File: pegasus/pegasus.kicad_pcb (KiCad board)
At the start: 2 copper layers, 1 part

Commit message: updated cache and added backup files
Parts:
- removed MPL3115A2: Altimeter, Adafruit_MPL3115A2:1x07
- added IC1: Adafruit_MPL3115A2, Adafruit_MPL3115A2:1x07, F.Cu at (139.7, 119.4)
- added IC2: Adafruit-BNO055-PCB, Adafruit_BNO055:adafruit_, F.Cu at (71.1, 85.2)
- added IC3: L70B-M39, Quectel_L70B-M39:1x18, F.Cu at (165.1, 111.8)
- added IC4: RFD900, RFD900:1x28, F.Cu at (161.8, 67.6)
- added J1: Conn_01x02_Female, Connector_PinHeader_2.00mm:PinHeader_1x02_P2.00mm_Horizontal, F.Cu at (88.9, 127.0)
- added J2: Conn_01x02_Female, Connector_PinHeader_2.00mm:PinHeader_1x02_P2.00mm_Horizontal, F.Cu at (78.7, 106.7)
- added J3: Conn_01x02_Female, Connector_PinHeader_2.00mm:PinHeader_1x02_P2.00mm_Horizontal, F.Cu at (94.0, 109.2)
- added U1: Teensy4.1, Teensy_4.1:Teensy_4.1, F.Cu at (114.3, 48.3)

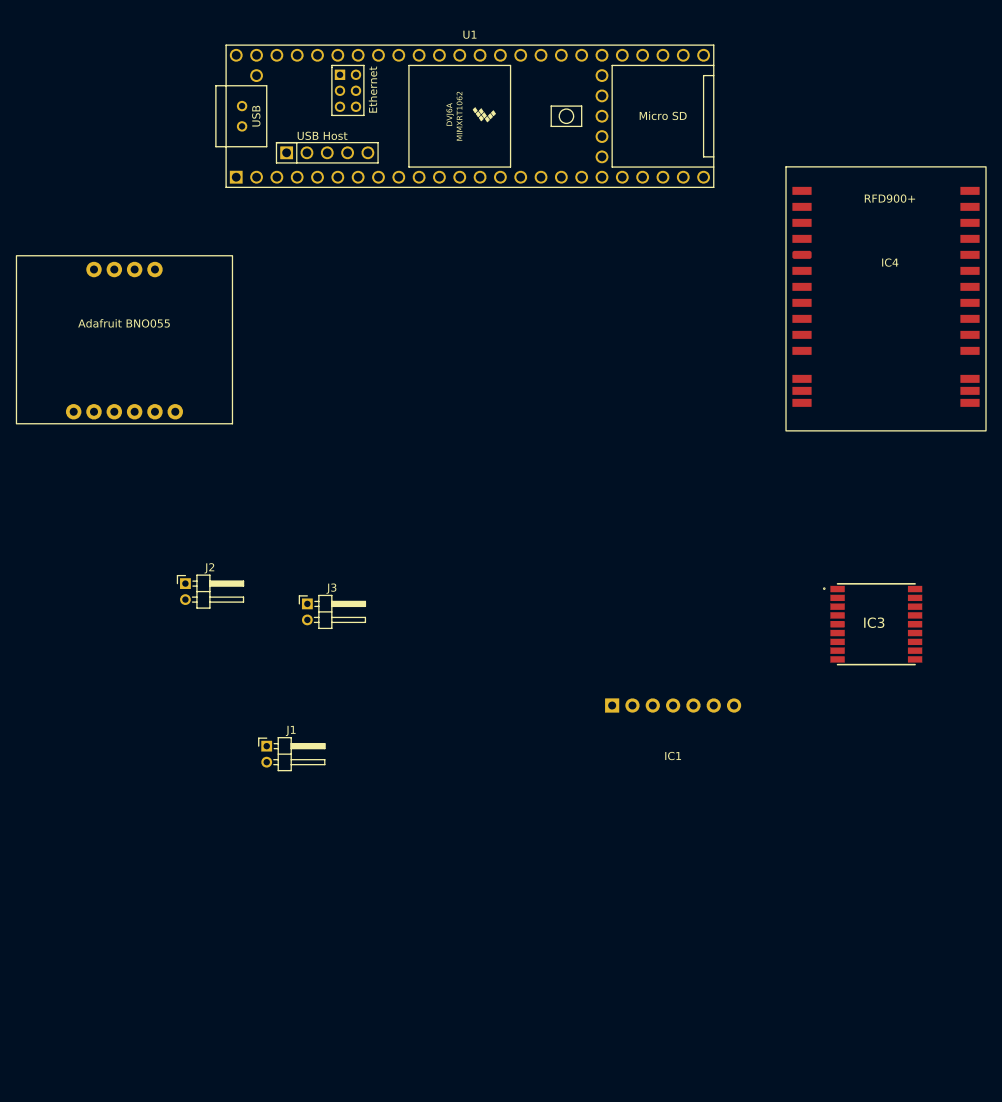
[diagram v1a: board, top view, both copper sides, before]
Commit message: outlined approximate geometry of pcb and made some connections
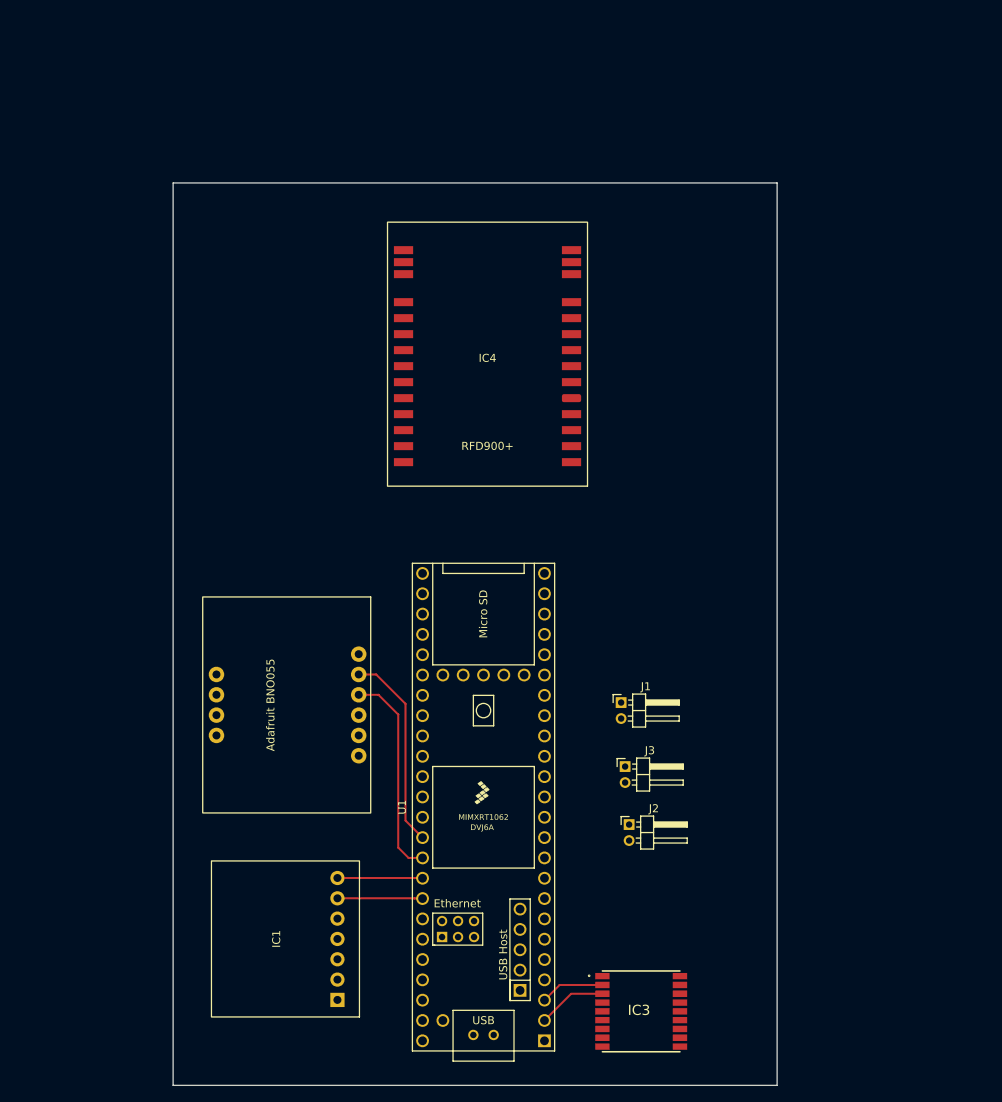
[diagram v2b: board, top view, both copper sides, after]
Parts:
- moved U1 86.4 mm to (116.0, 134.6), turned to 90 degrees
- moved J2 63.1 mm to (134.2, 136.8)
- moved IC3 56.6 mm to (135.7, 160.2)
- moved IC1 54.6 mm to (95.2, 151.1), turned to 90 degrees
- moved IC2 46.9 mm to (100.4, 121.8), turned to 90 degrees
- moved J1 44.6 mm to (133.2, 121.5)
- moved J3 44.6 mm to (133.7, 129.6)
- moved IC4 43.1 mm to (121.0, 81.5), turned to 180 degrees
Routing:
- net Net-(IC2-Pad4)_1: track 0.00 -> 26.2 mm
- net Net-(IC2-Pad5)_1: track 0.00 -> 25.0 mm
- net Net-(IC1-Pad7): track 0.00 -> 10.7 mm
- net Net-(IC1-Pad6): track 0.00 -> 10.7 mm
- net Net-(IC3-Pad3): track 0.00 -> 8.62 mm
- net Net-(IC3-Pad2): track 0.00 -> 8.02 mm
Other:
- board outline added: 75.5 x 112.8 mm

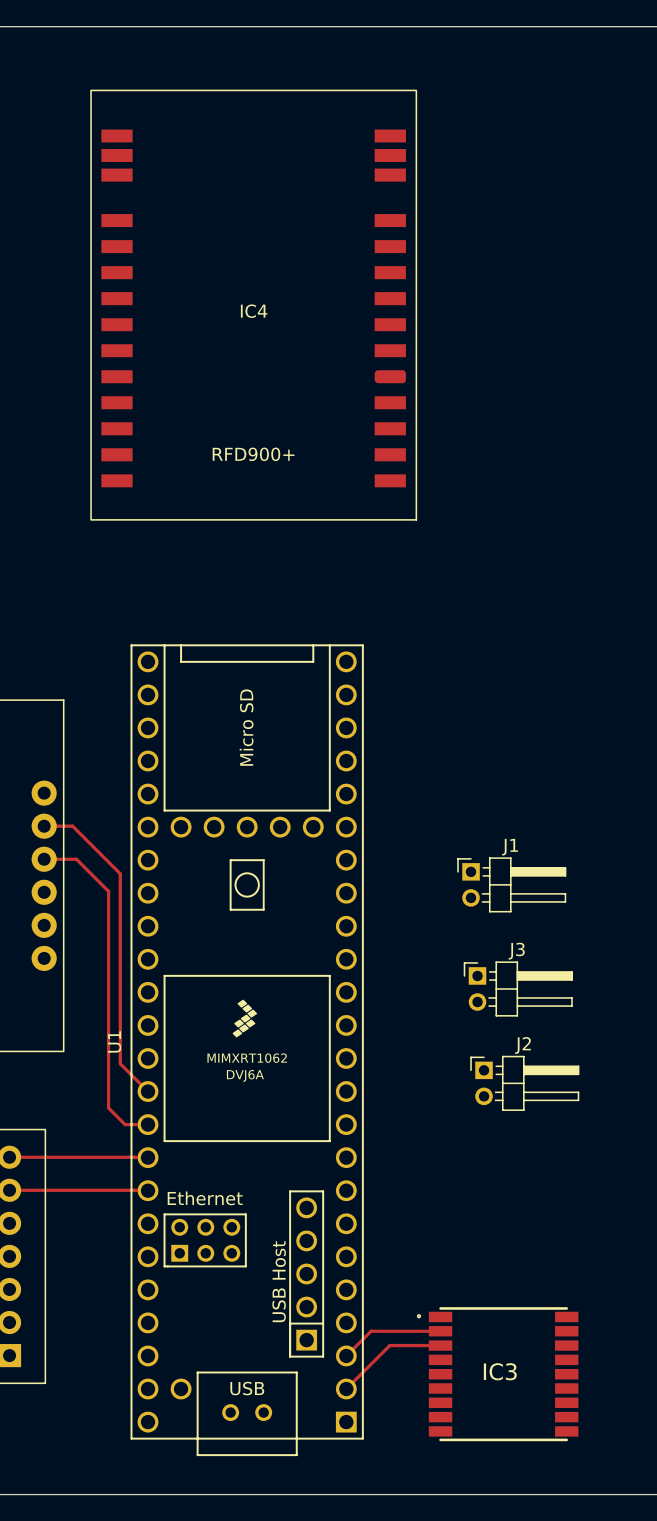
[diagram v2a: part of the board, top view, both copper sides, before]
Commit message: changed connector footprints from horizontal to vertical
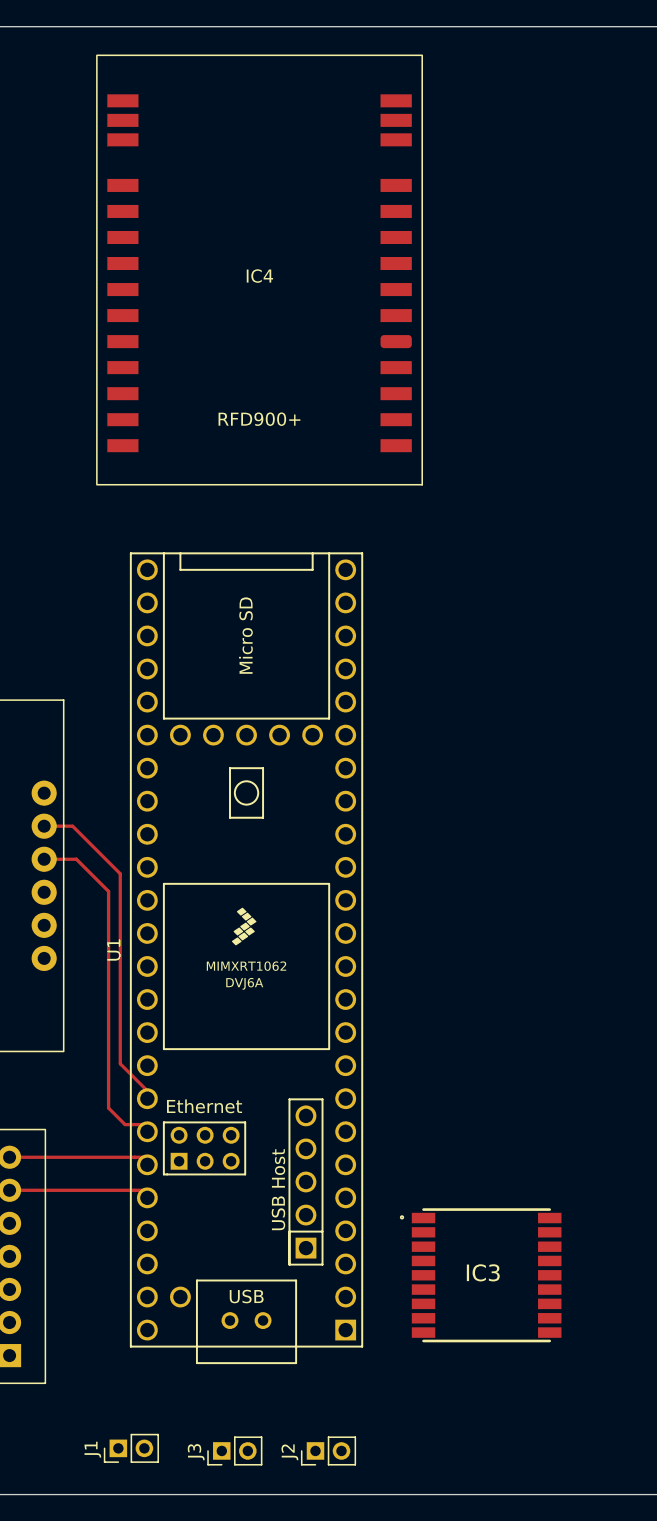
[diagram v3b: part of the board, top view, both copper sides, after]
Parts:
- J1, J2, J3: footprint Connector_PinHeader_2.00mm:PinHeader_1x02_P2.00mm_Horizontal -> Connector_PinHeader_2.00mm:PinHeader_1x02_P2.00mm_Vertical
- moved J1 51.9 mm to (106.1, 165.8), turned to 90 degrees
- moved J3 41.5 mm to (114.0, 166.1), turned to 90 degrees
- moved J2 32.0 mm to (121.2, 166.1), turned to 90 degrees
- moved IC3 7.71 mm to (134.4, 152.6)
- moved U1 7.07 mm to (116.0, 127.5)
- moved IC4 2.74 mm to (121.5, 78.8)
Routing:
- net unconnected-(U1-Pad44): track 0.00 -> 10.7 mm
- net unconnected-(U1-Pad43): track 0.00 -> 10.7 mm
- net Net-(IC1-Pad7): track 10.7 -> 0.00 mm
- net Net-(IC1-Pad6): track 10.7 -> 0.00 mm
- net Net-(IC3-Pad3): track 8.62 -> 0.00 mm
- net Net-(IC3-Pad2): track 8.02 -> 0.00 mm

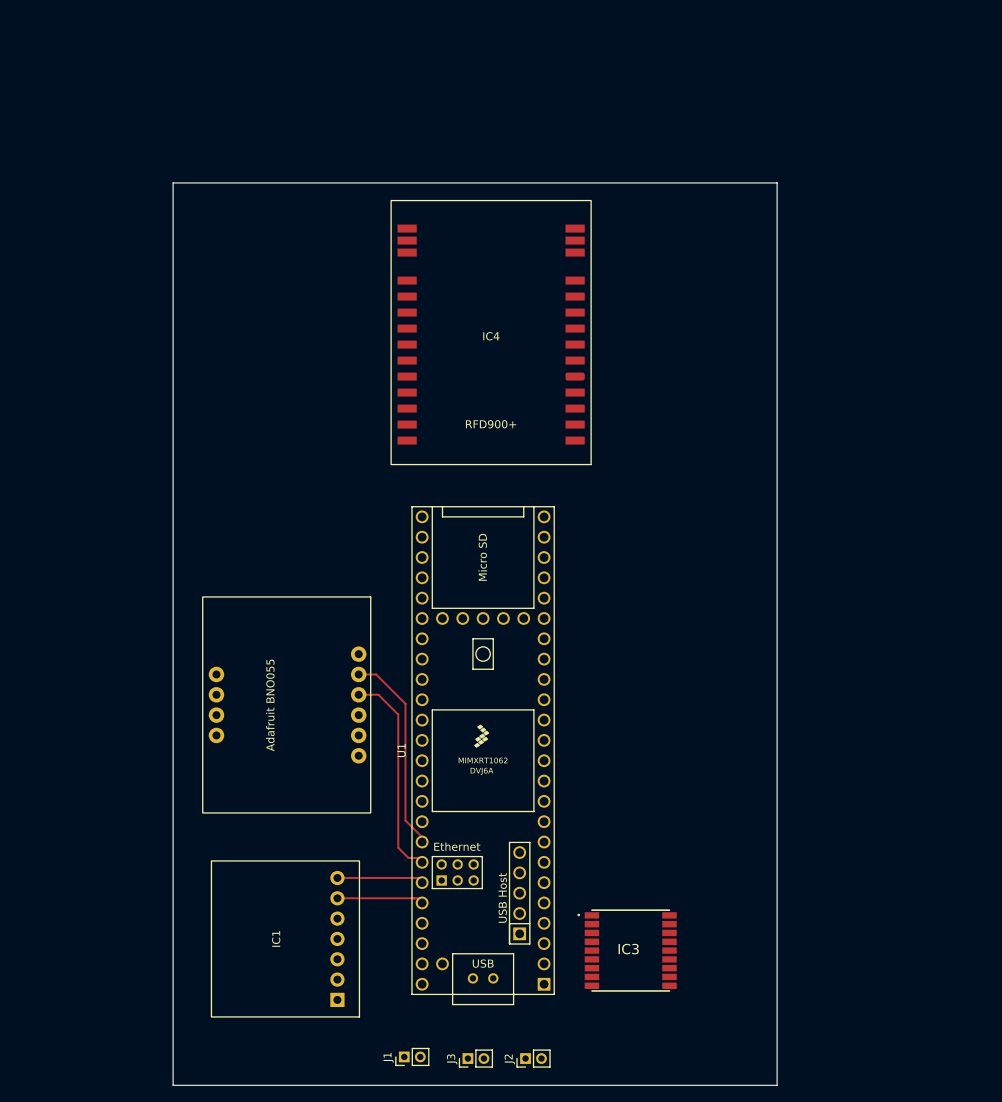
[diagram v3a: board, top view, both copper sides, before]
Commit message: adding sma coaxial connectors, footprint may change
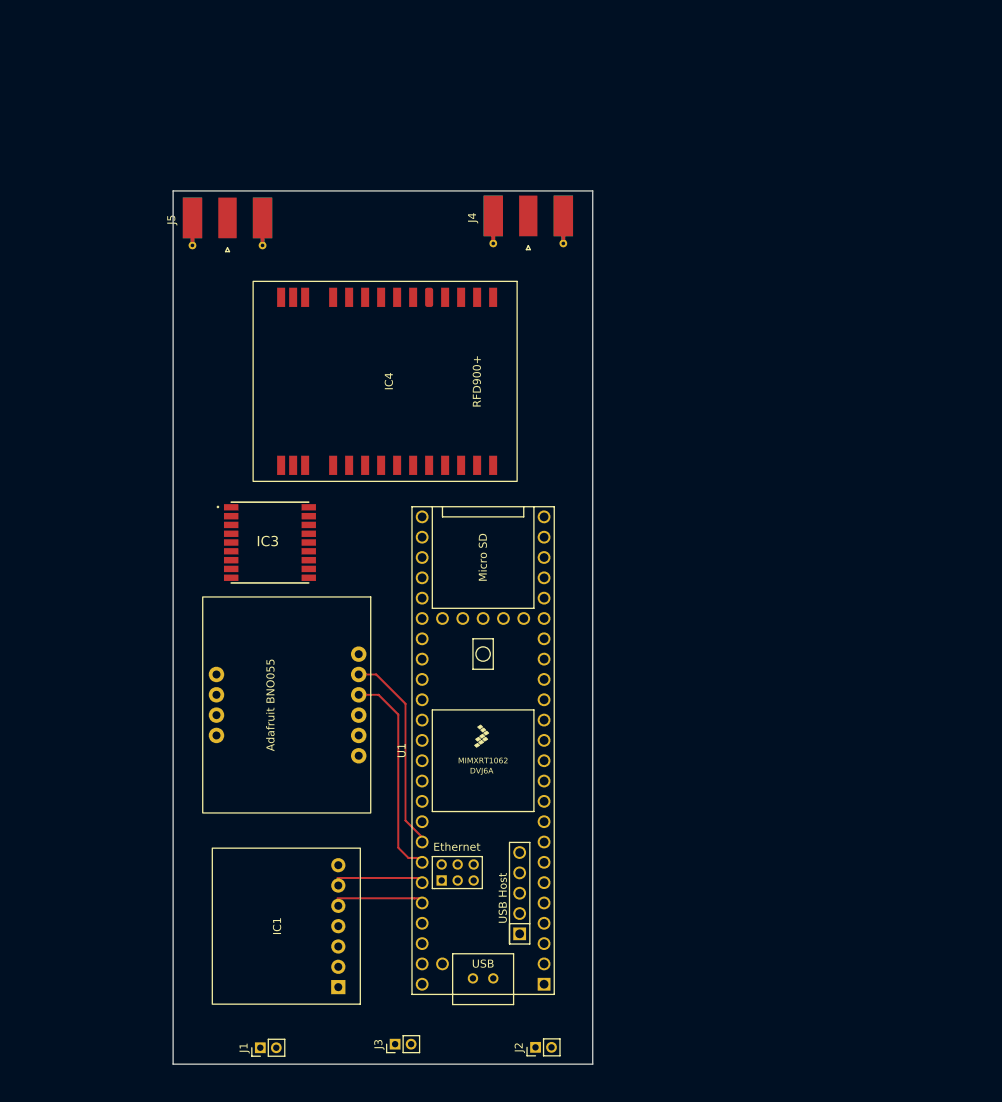
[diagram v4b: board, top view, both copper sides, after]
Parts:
- added J4: Conn_Coaxial, Connector_Coaxial:SMA_Molex_73251-1153_EdgeMount_Horizontal, F.Cu at (121.6, 62.4)
- added J5: Conn_Coaxial, Connector_Coaxial:SMA_Molex_73251-1153_EdgeMount_Horizontal, F.Cu at (84.0, 62.7)
- moved IC3 68.1 mm to (89.3, 101.5)
- moved J1 18.0 mm to (88.1, 164.7)
- moved IC4 14.4 mm to (107.2, 76.9), turned to -90 degrees
- moved J3 9.28 mm to (105.0, 164.2)
- moved J2 1.88 mm to (122.5, 164.7)
- moved IC1 1.60 mm to (95.3, 149.5)
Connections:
- IC4 pad 12: unconnected-(IC4-Pad12) -> Net-(IC4-Pad12)
- IC4 pad 13: unconnected-(IC4-Pad13) -> Net-(IC4-Pad13)
- IC4 pad 14: unconnected-(IC4-Pad14) -> Net-(IC4-Pad12)
- IC4 pad 15: unconnected-(IC4-Pad15) -> Net-(IC4-Pad15)
- IC4 pad 16: unconnected-(IC4-Pad16) -> Net-(IC4-Pad16)
- IC4 pad 17: unconnected-(IC4-Pad17) -> Net-(IC4-Pad15)
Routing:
- net unconnected-(U1-Pad42): track 0.00 -> 26.2 mm
- net Net-(IC2-Pad4)_1: track 26.2 -> 0.00 mm
- net unconnected-(U1-Pad44): track 10.7 -> 0.00 mm
- net unconnected-(U1-Pad43): track 10.7 -> 0.00 mm
- net unconnected-(IC1-Pad5): track 0.00 -> 10.7 mm
- net Net-(IC1-Pad6): track 0.00 -> 10.7 mm
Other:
- board size 75.5 x 112.8 mm -> 52.5 x 109.2 mm

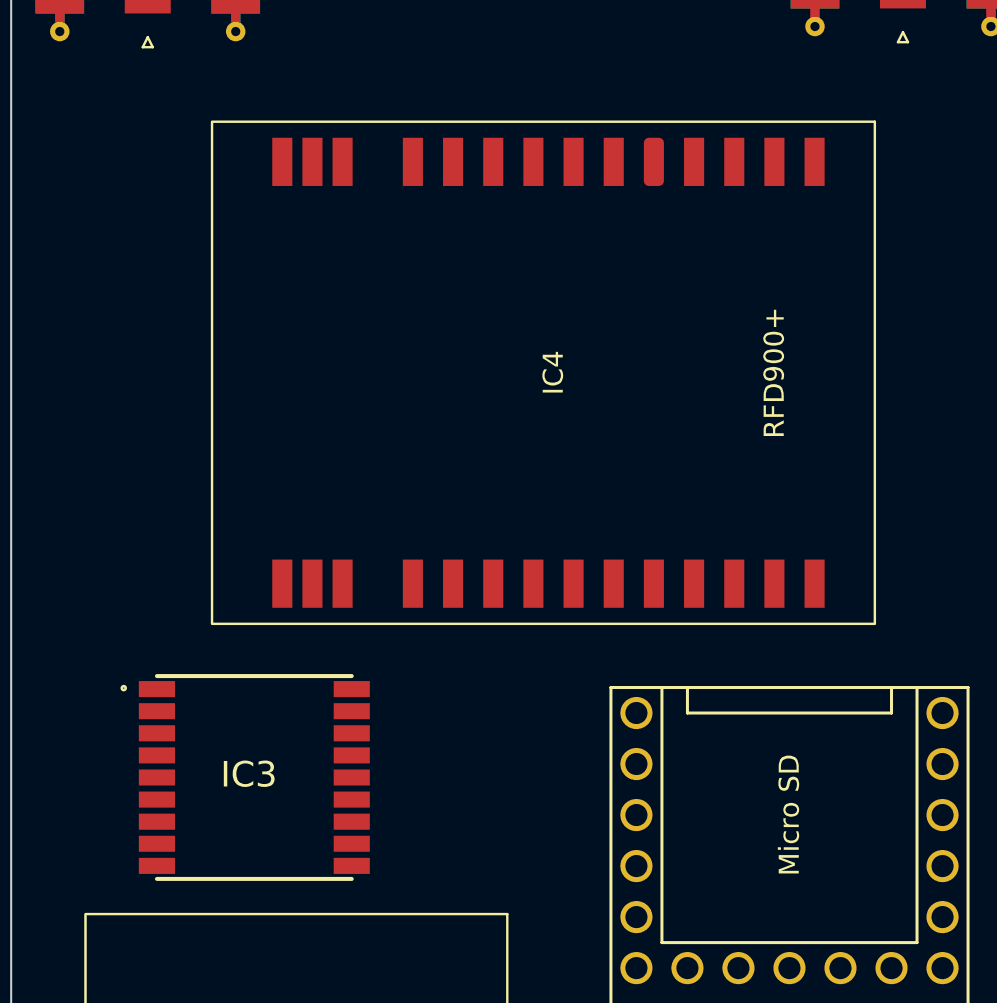
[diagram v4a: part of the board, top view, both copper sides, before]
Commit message: matched RFD900 footprint borders with datasheet
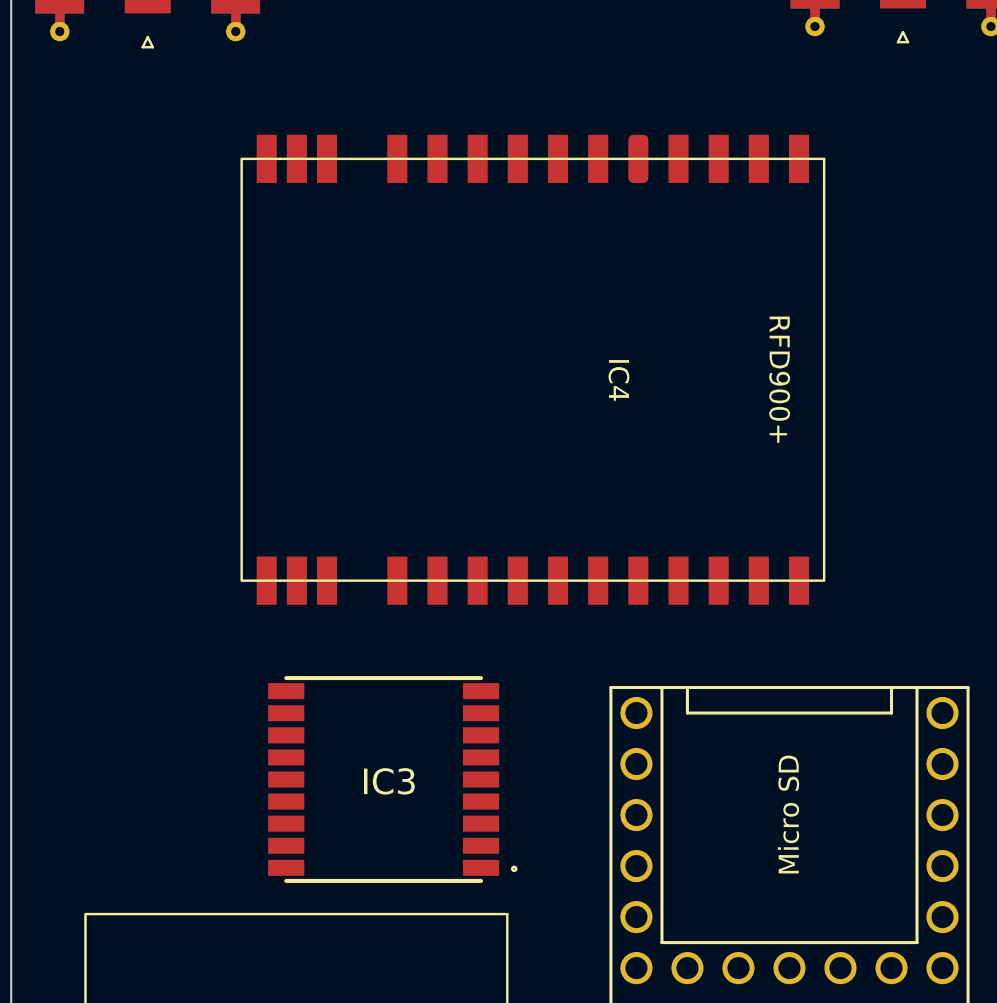
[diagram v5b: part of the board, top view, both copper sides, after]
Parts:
- moved IC3 6.44 mm to (95.7, 101.7), turned to 180 degrees
- moved IC4 0.79 mm to (106.4, 76.8)
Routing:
- net unconnected-(U1-Pad42): track 26.2 -> 0.00 mm
- net Net-(IC2-Pad4)_1: track 0.00 -> 26.2 mm
- net unconnected-(U1-Pad44): track 0.00 -> 10.7 mm
- net unconnected-(U1-Pad43): track 0.00 -> 10.7 mm
- net unconnected-(IC1-Pad5): track 10.7 -> 0.00 mm
- net Net-(IC1-Pad6): track 10.7 -> 0.00 mm
